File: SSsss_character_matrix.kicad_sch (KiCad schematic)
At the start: 17 parts, among them U15 SN74LVC244A, U16 SM411006N/15, U17 SM411006N/15, U18 SN74LVC244A, U19 SM411006N/15, U20 SM411006N/15, U21 SM411006N/15

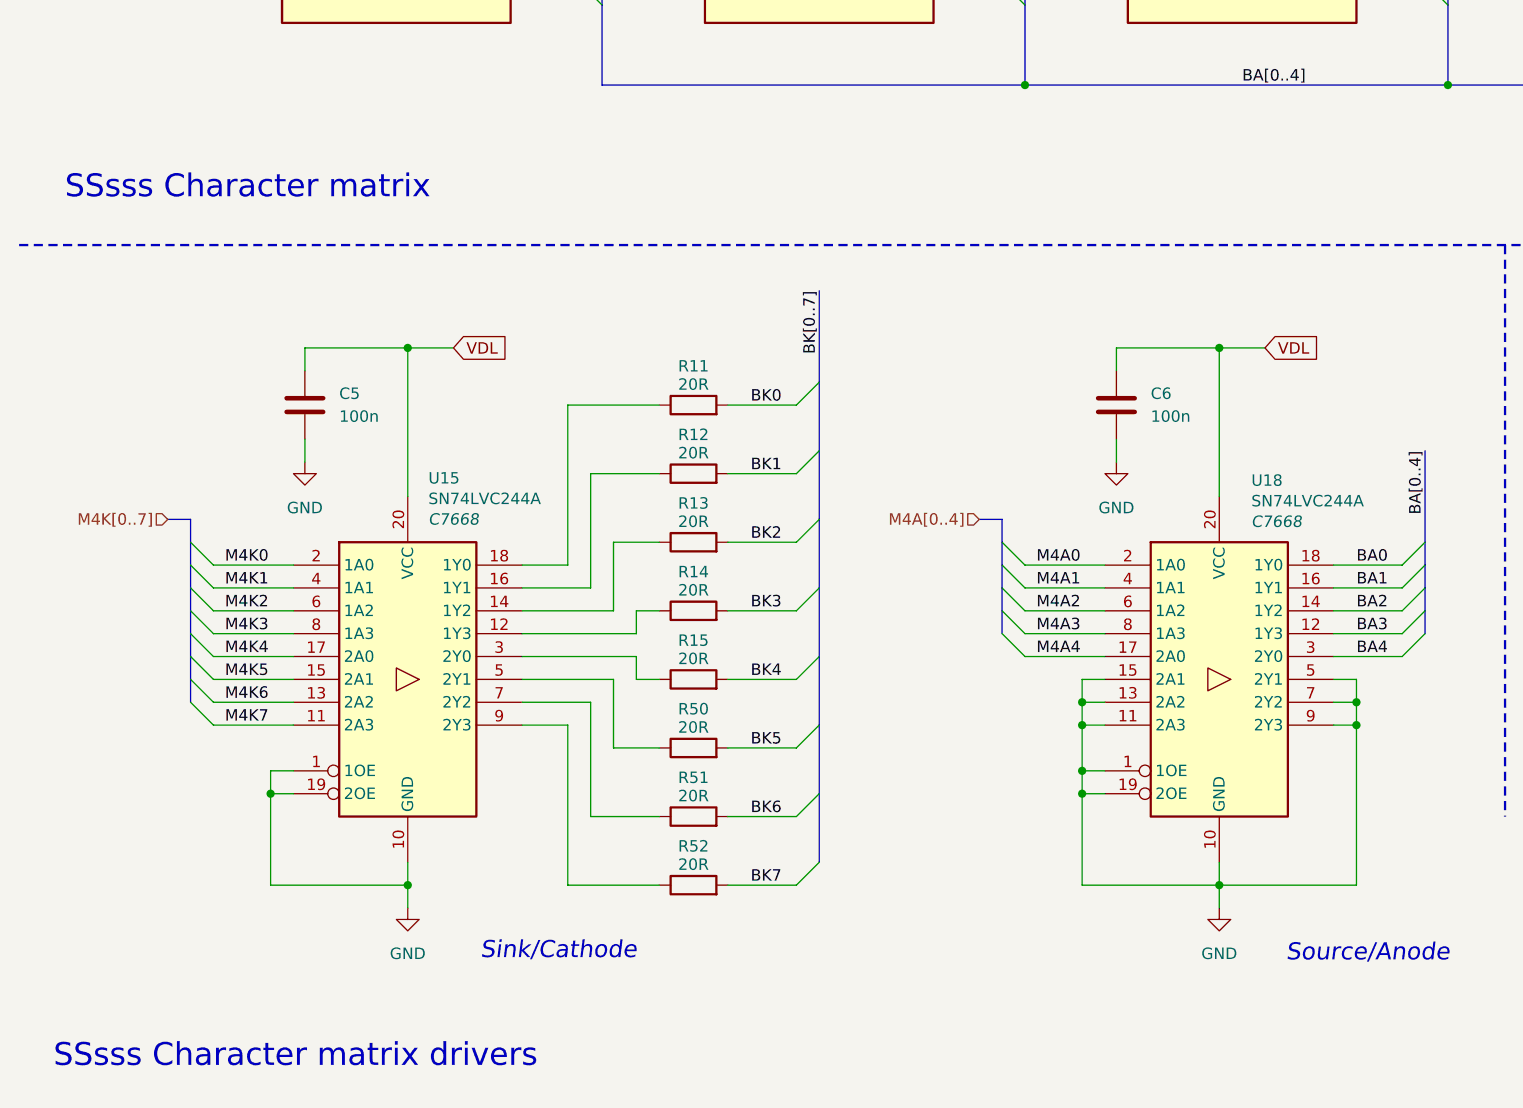
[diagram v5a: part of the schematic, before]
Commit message: verification
- sensor schematic verification
- change in the value of current limiting resistor
- disconnected unused buffer pins
- labeling or peripherals used in primary MCU
- additional user button
- DRC corrections
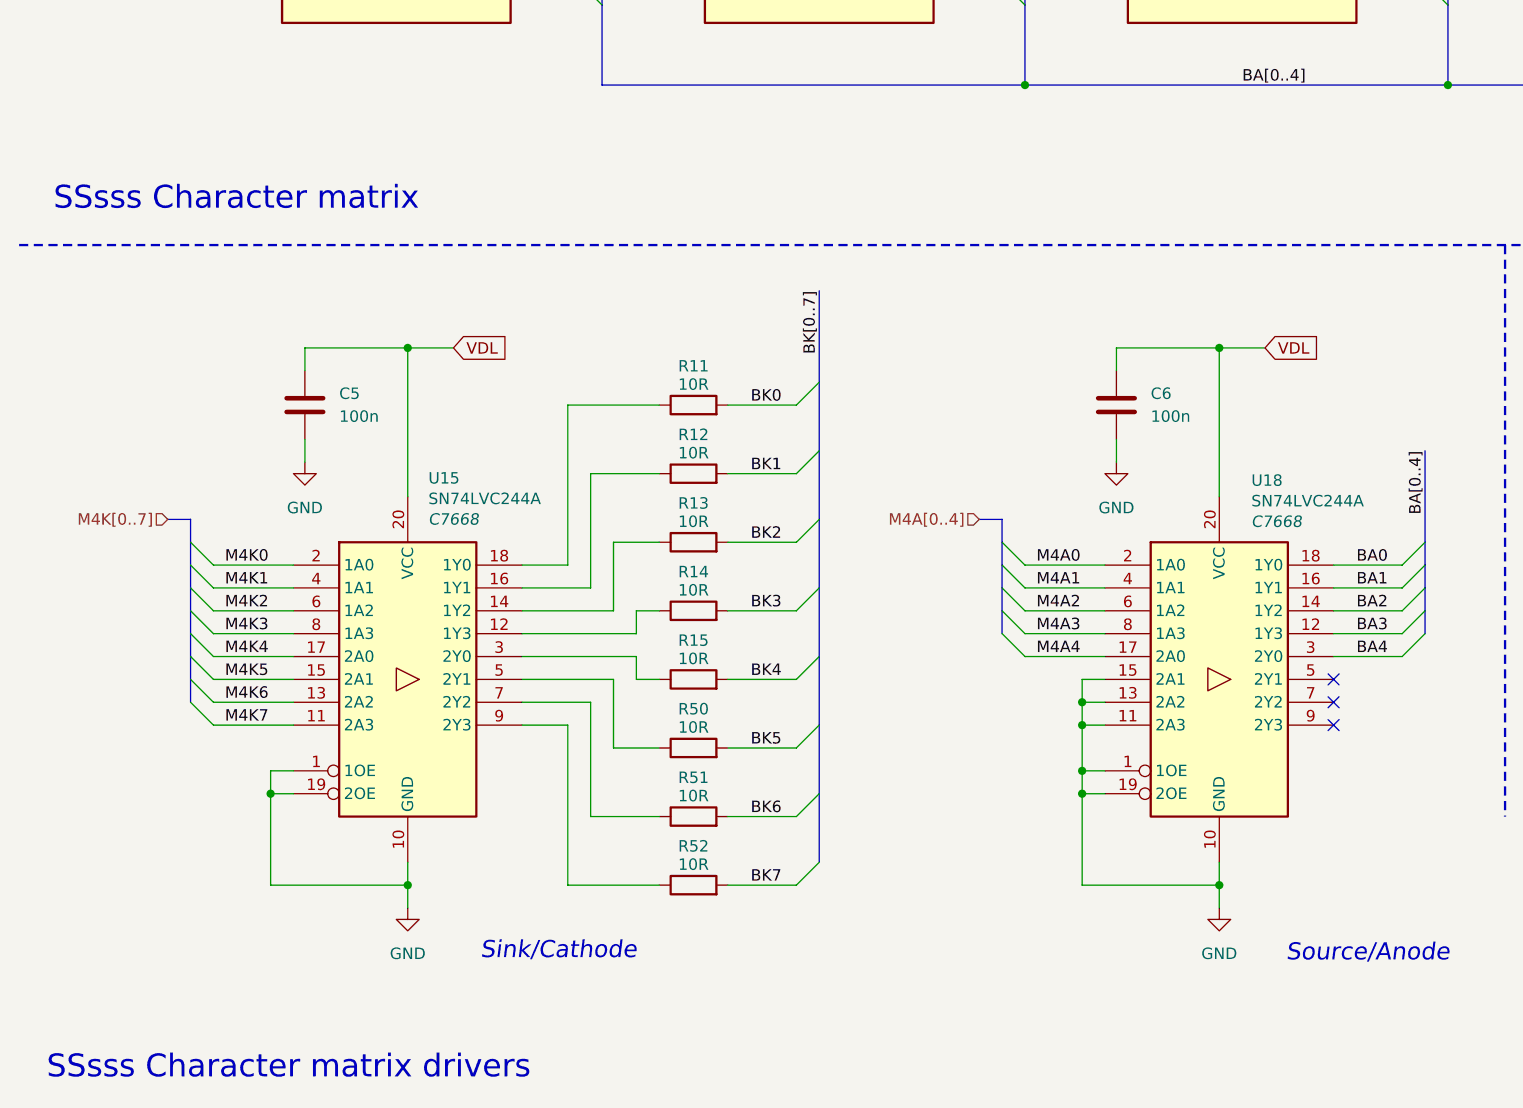
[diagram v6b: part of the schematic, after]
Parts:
- R11, R12, R13, R14, R15, R50, R51, R52: value 20R -> 10R
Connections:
- net GND: no longer U18.5 (2Y1), U18.7 (2Y2), U18.9 (2Y3)
- no-connect marks 0 -> 3
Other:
- company: Rajath Katker -> TJ71PL
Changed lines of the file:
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@@
 	(title_block
 		(title "SSsss Character Matrix & Drivers ")
-		(date "2025-11-04")
+		(date "2025-09-05")
 		(rev "v0.0")
-		(company "Rajath Katker")
+		(company "TJ71PL")
+		(comment 1 "天計")
 		(comment 4 "Final verification pending")
 	)
@@
 	(text "SSsss Character matrix"
 		(exclude_from_sim no)
-		(at 17.78 95.25 0)
+		(at 16.51 96.52 0)
 		(effects
 			(font
@@
 	(text "SSsss Character matrix drivers "
 		(exclude_from_sim no)
-		(at 16.51 191.77 0)
+		(at 15.748 193.04 0)
 		(effects
 			(font
@@
 	)
 	(junction
-		(at 161.29 152.4)
-		(diameter 0)
-		(color 0 0 0 0)
-	)
-	(junction
 		(at 146.05 172.72)
 		(diameter 0)
@@
 	)
 	(junction
-		(at 161.29 154.94)
-		(diameter 0)
-		(color 0 0 0 0)
-	)
-	(junction
 		(at 130.81 160.02)
 		(diameter 0)
@@
 		(color 0 0 0 0)
 	)
+	(no_connect
+		(at 158.75 154.94)
+	)
+	(no_connect
+		(at 158.75 152.4)
+	)
+	(no_connect
+		(at 158.75 149.86)
+	)
 	(bus_entry
 		(at 31.75 67.31)
@@
 		)
 	)
-	(wire
-		(pts
-			(xy 161.29 172.72) (xy 146.05 172.72)
-		)
-		(stroke
-			(width 0)
-			(type default)
-		)
-	)
 	(bus
 		(pts
@@
 		)
 	)
-	(wire
-		(pts
-			(xy 158.75 152.4) (xy 161.29 152.4)
-		)
-		(stroke
-			(width 0)
-			(type default)
-		)
-	)
 	(bus
 		(pts
@@
 	(wire
 		(pts
-			(xy 158.75 149.86) (xy 161.29 149.86)
-		)
-		(stroke
-			(width 0)
-			(type default)
-		)
-	)
-	(wire
-		(pts
 			(xy 175.26 62.23) (xy 180.34 62.23)
 		)
@@
 		)
 	)
-	(wire
-		(pts
-			(xy 161.29 152.4) (xy 161.29 154.94)
-		)
-		(stroke
-			(width 0)
-			(type default)
-		)
-	)
 	(bus
 		(pts
@@
 		)
 	)
-	(wire
-		(pts
-			(xy 161.29 154.94) (xy 161.29 172.72)
-		)
-		(stroke
-			(width 0)
-			(type default)
-		)
-	)
 	(bus
 		(pts
@@
 		)
 	)
-	(wire
-		(pts
-			(xy 161.29 149.86) (xy 161.29 152.4)
-		)
-		(stroke
-			(width 0)
-			(type default)
-		)
-	)
 	(bus
 		(pts
@@
 	(wire
 		(pts
-			(xy 158.75 154.94) (xy 161.29 154.94)
-		)
-		(stroke
-			(width 0)
-			(type default)
-		)
-	)
-	(wire
-		(pts
 			(xy 81.28 149.86) (xy 83.82 149.86)
 		)
@@
 			)
 		)
-		(property "Value" "20R"
+		(property "Value" "10R"
 			(at 87.63 155.194 90)
 			(effects
@@
 			)
 		)
-		(property "Value" "20R"
+		(property "Value" "10R"
 			(at 87.63 124.714 90)
 			(effects
@@
 			)
 		)
-		(property "Value" "20R"
+		(property "Value" "10R"
 			(at 87.63 162.814 90)
 			(effects
@@
 			)
 		)
-		(property "Value" "20R"
+		(property "Value" "10R"
 			(at 87.63 117.094 90)
 			(effects
@@
 			)
 		)
-		(property "Value" "20R"
+		(property "Value" "10R"
 			(at 87.63 147.574 90)
 			(effects
@@
 			)
 		)
-		(property "Value" "20R"
+		(property "Value" "10R"
 			(at 87.63 170.434 90)
 			(effects
@@
 			)
 		)
-		(property "Value" "20R"
+		(property "Value" "10R"
 			(at 87.63 132.334 90)
 			(effects
@@
 			)
 		)
-		(property "Value" "20R"
+		(property "Value" "10R"
 			(at 87.63 139.954 90)
 			(effects

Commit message: semi final verification
- change in display type to common cathode
- verification of the schematic
- addition of footprints
- further minor changes
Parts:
- removed U16, U17, U19, U20, U21: SM411006N/15, precision_clock:SM411006N15, symbol precision_clock:SM411006N/15
- added U16, U17, U19, U20, U21: 10016AS, precision_clock:10016AS, symbol precision_clock:10016AS
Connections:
- net BA0: now also R11.2, U16.7 (A), U17.7 (A), U19.7 (A), U21.7 (A); no longer U18.18 (1Y0)
- net BA1: now also R12.2, U16.6 (B), U17.6 (B), U19.6 (B), U20.6 (B), U20.7 (A), U21.6 (B); no longer U18.16 (1Y1)
- net BA2: now also R13.2, U16.4 (C), U17.4 (C), U19.4 (C), U20.4 (C), U21.4 (C); no longer U18.14 (1Y2)
- net BA3: now also R14.2, U16.2 (D), U17.2 (D), U19.2 (D), U20.2 (D), U21.2 (D); no longer U18.12 (1Y3)
- net BA4: now also R15.2, U16.1 (E), U17.1 (E), U19.1 (E), U20.1 (E), U21.1 (E); no longer U18.3 (2Y0)
- net BK0: now also U18.18 (1Y0), U16.3 (CK), U16.8 (CK); no longer R11.2
- net BK1: now also U18.16 (1Y1), U17.3 (CK), U17.8 (CK); no longer R12.2
- net BK2: now also U18.14 (1Y2), U19.3 (CK), U19.8 (CK); no longer R13.2
- net BK3: now also U18.12 (1Y3), U20.3 (CK), U20.8 (CK); no longer R14.2
- net BK4: now also U18.3 (2Y0), U21.3 (CK), U21.8 (CK); no longer R15.2
- net M4A0: now also U15.2 (1A0); no longer U18.2 (1A0)
- net M4A1: now also U15.4 (1A1); no longer U18.4 (1A1)
- net M4A2: now also U15.6 (1A2); no longer U18.6 (1A2)
- net M4A3: now also U15.8 (1A3); no longer U18.8 (1A3)
- net M4A4: now also U15.17 (2A0); no longer U18.17 (2A0)
- net M4K0: now also U18.2 (1A0); no longer U15.2 (1A0)
- net M4K1: now also U18.4 (1A1); no longer U15.4 (1A1)
- net M4K2: now also U18.6 (1A2); no longer U15.6 (1A2)
- net M4K3: now also U18.8 (1A3); no longer U15.8 (1A3)
- net M4K4: now also U18.17 (2A0); no longer U15.17 (2A0)
- net BK5 renamed BA5
- net BA5: now also U16.9 (F), U17.9 (F), U19.9 (F), U20.9 (F), U21.9 (F)
- net BK6 renamed BA6
- net BA6: now also U16.10 (G), U17.10 (G), U19.10 (G), U20.10 (G), U21.10 (G)
- net BK7 renamed BA7
- net BA7: now also U16.5 (DP), U17.5 (DP), U19.5 (DP), U20.5 (DP), U21.5 (DP)
- net M4K5 renamed M4A5
- net M4K6 renamed M4A6
- net M4K7 renamed M4A7
